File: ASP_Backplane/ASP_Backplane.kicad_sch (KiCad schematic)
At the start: 168 parts, among them J1 ADC-010-1, J10 250Hz, J11 125Hz, J12 63Hz, J13 32Hz, J2 FC681374V, J3 FC681374V, J4 16kHz, J5 8kHz, J6 4kHz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

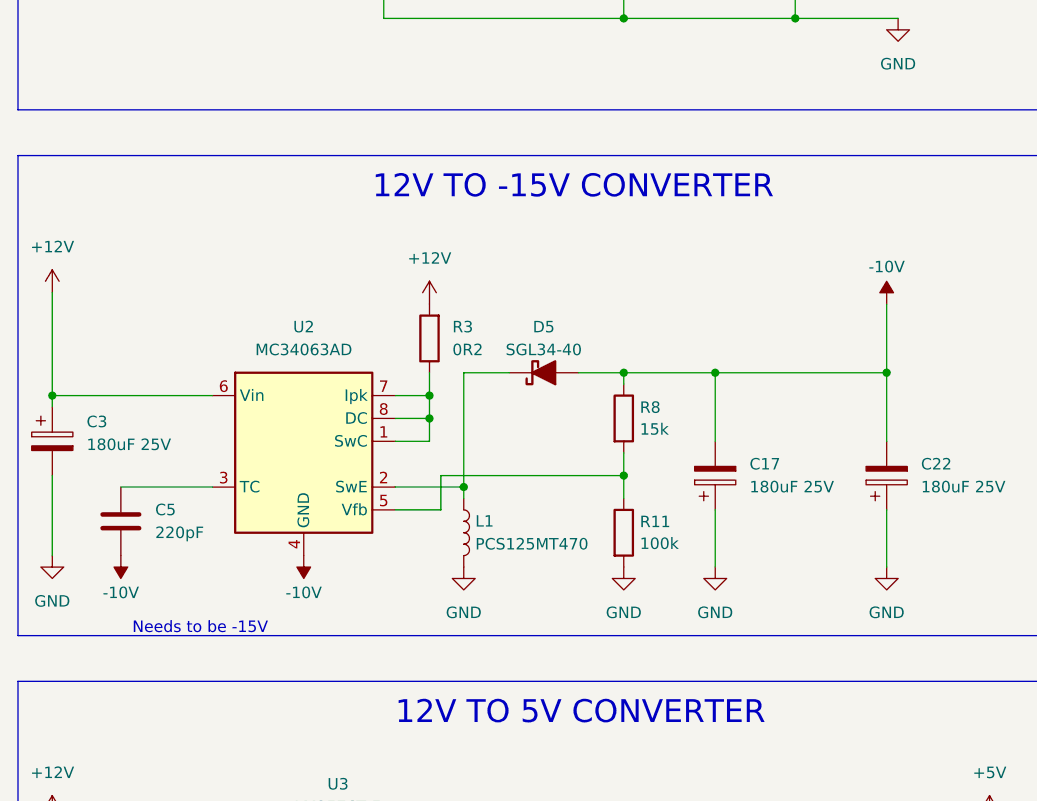
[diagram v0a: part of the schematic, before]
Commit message: Add documentation pictures
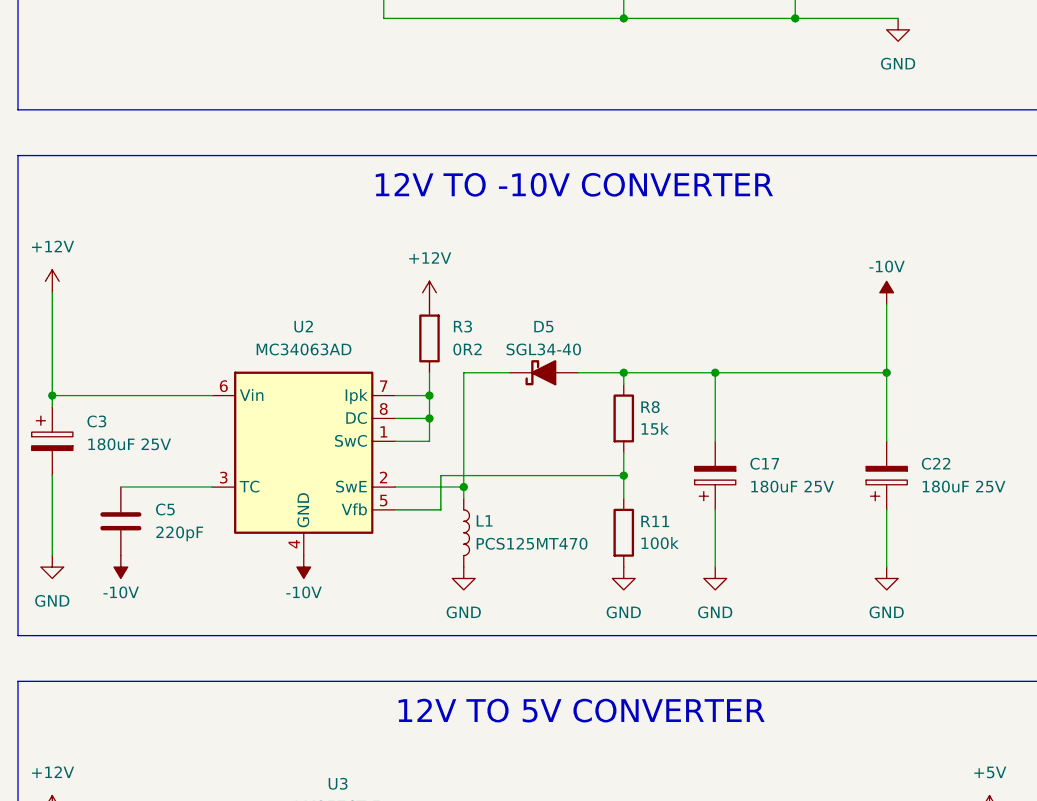
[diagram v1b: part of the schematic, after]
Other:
- note added: "12V TO -10V CONVERTER"
- note removed: "12V TO -15V CONVERTER"
- note removed: "Needs to be -15V"
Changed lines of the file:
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@@
     (effects (font (size 1.27 1.27)) (justify left bottom))
   )
-  (text "12V TO -15V CONVERTER" (at 53.34 134.62 0)
+  (text "12V TO -10V CONVERTER" (at 53.34 134.62 0)
     (effects (font (size 2.54 2.54)) (justify left bottom))
   )
@@
     (effects (font (size 1.27 1.27)) (justify left bottom))
   )
-  (text "Needs to be -15V" (at 26.67 182.88 0)
-    (effects (font (size 1.27 1.27)) (justify left bottom))
-  )
